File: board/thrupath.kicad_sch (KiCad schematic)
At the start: 114 parts, among them J6 BEL_FUSE_0826-1G1T-23-F, J7 BEL_FUSE_0826-1G1T-23-F, U4 XC7S15-1FTGB196C, U5 KSZ9031RN, U6 KSZ9031RN, U7 ECS-2016MVQ-250-CN-TR, U8 ECS-2016MVQ-250-CN-TR

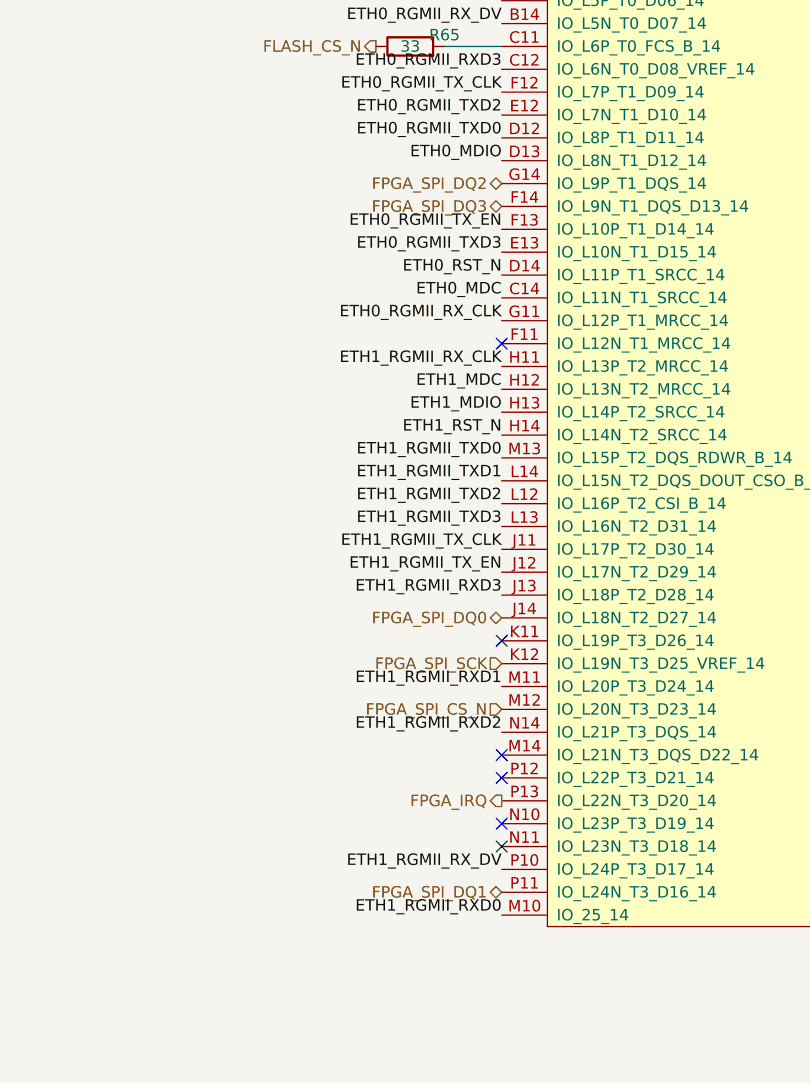
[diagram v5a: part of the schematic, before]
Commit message: Updating file: ethernet-tap.kicad_pcb with current fully routed design.
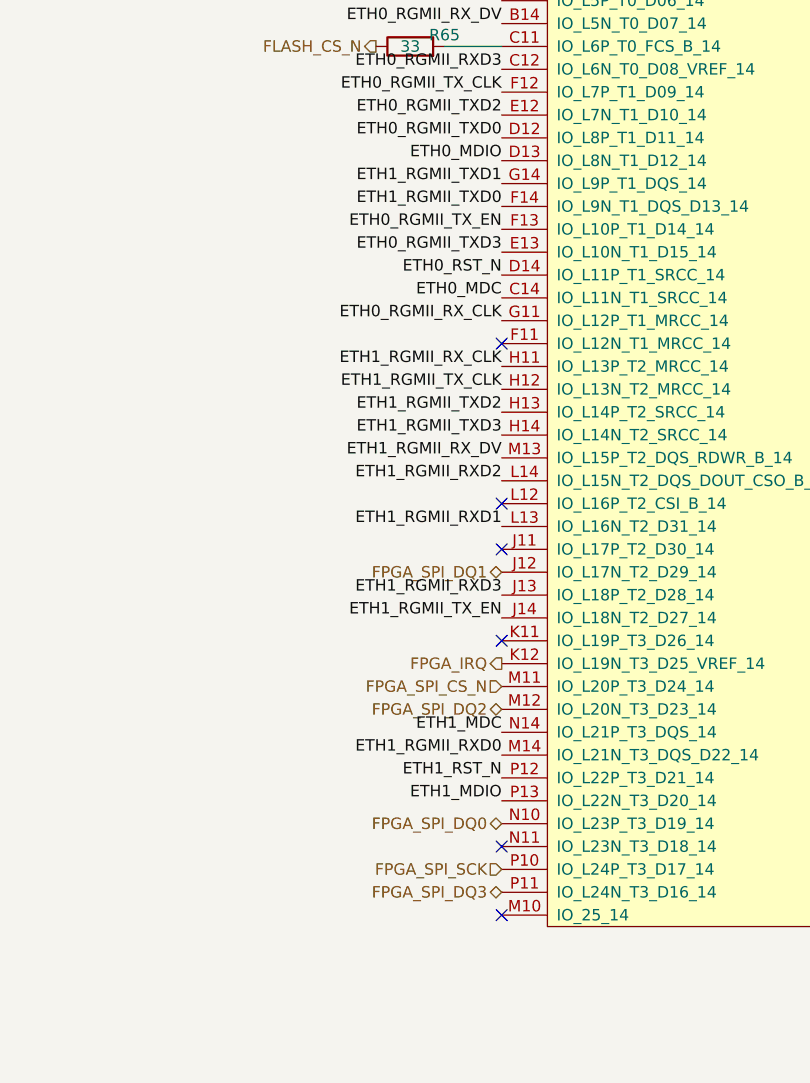
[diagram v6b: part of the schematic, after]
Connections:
- net ETH1_MDC: now also U4.N14 (IO_L21P_T3_DQS_14); no longer U4.H12 (IO_L13N_T2_MRCC_14)
- net ETH1_MDIO: now also U4.P13 (IO_L22N_T3_D20_14); no longer U4.H13 (IO_L14P_T2_SRCC_14)
- net ETH1_RGMII_RXD0: now also U4.M14 (IO_L21N_T3_DQS_D22_14); no longer U4.M10 (IO_25_14)
- net ETH1_RGMII_RXD1: now also U4.L13 (IO_L16N_T2_D31_14); no longer U4.M11 (IO_L20P_T3_D24_14)
- net ETH1_RGMII_RXD2: now also U4.L14 (IO_L15N_T2_DQS_DOUT_CSO_B_14); no longer U4.N14 (IO_L21P_T3_DQS_14)
- net ETH1_RGMII_RX_DV: now also U4.M13 (IO_L15P_T2_DQS_RDWR_B_14); no longer U4.P10 (IO_L24P_T3_D17_14)
- net ETH1_RGMII_TXD0: now also U4.F14 (IO_L9N_T1_DQS_D13_14); no longer U4.M13 (IO_L15P_T2_DQS_RDWR_B_14)
- net ETH1_RGMII_TXD1: now also U4.G14 (IO_L9P_T1_DQS_14); no longer U4.L14 (IO_L15N_T2_DQS_DOUT_CSO_B_14)
- net ETH1_RGMII_TXD2: now also U4.H13 (IO_L14P_T2_SRCC_14); no longer U4.L12 (IO_L16P_T2_CSI_B_14)
- net ETH1_RGMII_TXD3: now also U4.H14 (IO_L14N_T2_SRCC_14); no longer U4.L13 (IO_L16N_T2_D31_14)
- net ETH1_RGMII_TX_CLK: now also U4.H12 (IO_L13N_T2_MRCC_14); no longer U4.J11 (IO_L17P_T2_D30_14)
- net ETH1_RGMII_TX_EN: now also U4.J14 (IO_L18N_T2_D27_14); no longer U4.J12 (IO_L17N_T2_D29_14)
- net ETH1_RST_N: now also U4.P12 (IO_L22P_T3_D21_14); no longer U4.H14 (IO_L14N_T2_SRCC_14)
- net FPGA_IRQ: now also U4.K12 (IO_L19N_T3_D25_VREF_14); no longer U4.P13 (IO_L22N_T3_D20_14)
- net FPGA_SPI_CS_N: now also U4.M11 (IO_L20P_T3_D24_14); no longer U4.M12 (IO_L20N_T3_D23_14)
- net FPGA_SPI_DQ0: now also U4.N10 (IO_L23P_T3_D19_14); no longer U4.J14 (IO_L18N_T2_D27_14)
- net FPGA_SPI_DQ1: now also U4.J12 (IO_L17N_T2_D29_14); no longer U4.P11 (IO_L24N_T3_D16_14)
- net FPGA_SPI_DQ2: now also U4.M12 (IO_L20N_T3_D23_14); no longer U4.G14 (IO_L9P_T1_DQS_14)
- net FPGA_SPI_DQ3: now also U4.P11 (IO_L24N_T3_D16_14); no longer U4.F14 (IO_L9N_T1_DQS_D13_14)
- net FPGA_SPI_SCK: now also U4.P10 (IO_L24P_T3_D17_14); no longer U4.K12 (IO_L19N_T3_D25_VREF_14)
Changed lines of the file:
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@@
   (title_block
     (title "Active 10/100/1000baseT Tap")
-    (date "2022-12-24")
+    (date "2022-12-26")
     (rev "0.1")
     (company "Antikernel Labs")
@@
   )
   (no_connect (at 143.51 165.1))
+  (no_connect (at 364.49 99.06))
+  (no_connect (at 364.49 137.16))
   (no_connect (at 143.51 176.53))
-  (no_connect (at 364.49 134.62))
   (no_connect (at 143.51 87.63))
   (no_connect (at 364.49 35.56))
-  (no_connect (at 364.49 127))
-  (no_connect (at 364.49 129.54))
   (no_connect (at 364.49 114.3))
-  (no_connect (at 364.49 137.16))
+  (no_connect (at 364.49 104.14))
   (no_connect (at 364.49 81.28))
   (no_connect (at 86.36 157.48))
+  (no_connect (at 364.49 144.78))
   (no_connect (at 364.49 33.02))
   (no_connect (at 143.51 76.2))
@@
     (effects (font (size 1.27 1.27)) (justify left bottom))
   )
-  (label "ETH1_RGMII_TXD1" (at 364.49 96.52 180)
+  (label "ETH1_RGMII_TXD1" (at 364.49 63.5 180)
     (effects (font (size 1.27 1.27)) (justify right bottom))
   )
@@
     (effects (font (size 1.27 1.27)) (justify left bottom))
   )
-  (label "ETH1_RGMII_TX_CLK" (at 364.49 104.14 180)
+  (label "ETH1_RGMII_TX_CLK" (at 364.49 86.36 180)
     (effects (font (size 1.27 1.27)) (justify right bottom))
   )
@@
     (effects (font (size 1.27 1.27)) (justify right bottom))
   )
-  (label "ETH1_RST_N" (at 364.49 91.44 180)
+  (label "ETH1_RST_N" (at 364.49 129.54 180)
     (effects (font (size 1.27 1.27)) (justify right bottom))
   )
@@
     (effects (font (size 1.27 1.27)) (justify left bottom))
   )
-  (label "ETH1_RGMII_TXD0" (at 364.49 93.98 180)
+  (label "ETH1_RGMII_TXD0" (at 364.49 66.04 180)
     (effects (font (size 1.27 1.27)) (justify right bottom))
   )
@@
     (effects (font (size 1.27 1.27)) (justify right bottom))
   )
-  (label "ETH1_RGMII_RXD2" (at 364.49 124.46 180)
+  (label "ETH1_RGMII_RXD2" (at 364.49 96.52 180)
     (effects (font (size 1.27 1.27)) (justify right bottom))
   )
@@
     (effects (font (size 1.27 1.27)) (justify right bottom))
   )
-  (label "ETH1_MDC" (at 364.49 86.36 180)
+  (label "ETH1_MDC" (at 364.49 124.46 180)
     (effects (font (size 1.27 1.27)) (justify right bottom))
   )
@@
     (effects (font (size 1.27 1.27)) (justify right bottom))
   )
-  (label "ETH1_RGMII_RX_DV" (at 364.49 139.7 180)
+  (label "ETH1_RGMII_RX_DV" (at 364.49 93.98 180)
     (effects (font (size 1.27 1.27)) (justify right bottom))
   )
@@
     (effects (font (size 1.27 1.27)) (justify right bottom))
   )
-  (label "ETH1_RGMII_RXD1" (at 364.49 119.38 180)
+  (label "ETH1_RGMII_RXD1" (at 364.49 101.6 180)
     (effects (font (size 1.27 1.27)) (justify right bottom))
   )
@@
     (effects (font (size 1.27 1.27)) (justify left bottom))
   )
-  (label "ETH1_MDIO" (at 364.49 88.9 180)
+  (label "ETH1_MDIO" (at 364.49 132.08 180)
     (effects (font (size 1.27 1.27)) (justify right bottom))
   )
@@
     (effects (font (size 1.27 1.27)) (justify left bottom))
   )
-  (label "ETH1_RGMII_TX_EN" (at 364.49 106.68 180)
-    (effects (font (size 1.27 1.27)) (justify right bottom))
-  )
-  (label "ETH1_RGMII_TXD3" (at 364.49 101.6 180)
+  (label "ETH1_RGMII_TX_EN" (at 364.49 111.76 180)
+    (effects (font (size 1.27 1.27)) (justify right bottom))
+  )
+  (label "ETH1_RGMII_TXD3" (at 364.49 91.44 180)
     (effects (font (size 1.27 1.27)) (justify right bottom))
   )
@@
     (effects (font (size 1.27 1.27)) (justify right bottom))
   )
-  (label "ETH1_RGMII_TXD2" (at 364.49 99.06 180)
+  (label "ETH1_RGMII_TXD2" (at 364.49 88.9 180)
     (effects (font (size 1.27 1.27)) (justify right bottom))
   )
@@
     (effects (font (size 1.27 1.27)) (justify right bottom))
   )
-  (label "ETH1_RGMII_RXD0" (at 364.49 144.78 180)
+  (label "ETH1_RGMII_RXD0" (at 364.49 127 180)
     (effects (font (size 1.27 1.27)) (justify right bottom))
   )
@@
     (effects (font (size 1.27 1.27)) (justify right))
   )
-  (hierarchical_label "FPGA_SPI_CS_N" (shape input) (at 364.49 121.92 180)
+  (hierarchical_label "FPGA_SPI_CS_N" (shape input) (at 364.49 119.38 180)
     (effects (font (size 1.27 1.27)) (justify right))
   )
@@
     (effects (font (size 1.27 1.27)) (justify right))
   )
-  (hierarchical_label "FPGA_SPI_DQ2" (shape bidirectional) (at 364.49 63.5 180)
+  (hierarchical_label "FPGA_SPI_DQ2" (shape bidirectional) (at 364.49 121.92 180)
     (effects (font (size 1.27 1.27)) (justify right))
   )
-  (hierarchical_label "FPGA_SPI_DQ3" (shape bidirectional) (at 364.49 66.04 180)
+  (hierarchical_label "FPGA_SPI_DQ3" (shape bidirectional) (at 364.49 142.24 180)
     (effects (font (size 1.27 1.27)) (justify right))
   )
-  (hierarchical_label "FPGA_SPI_SCK" (shape input) (at 364.49 116.84 180)
+  (hierarchical_label "FPGA_SPI_SCK" (shape input) (at 364.49 139.7 180)
     (effects (font (size 1.27 1.27)) (justify right))
   )
-  (hierarchical_label "FPGA_IRQ" (shape output) (at 364.49 132.08 180)
+  (hierarchical_label "FPGA_IRQ" (shape output) (at 364.49 116.84 180)
     (effects (font (size 1.27 1.27)) (justify right))
   )
@@
     (effects (font (size 1.27 1.27)) (justify right))
   )
-  (hierarchical_label "FPGA_SPI_DQ1" (shape bidirectional) (at 364.49 142.24 180)
+  (hierarchical_label "FPGA_SPI_DQ1" (shape bidirectional) (at 364.49 106.68 180)
     (effects (font (size 1.27 1.27)) (justify right))
   )
-  (hierarchical_label "FPGA_SPI_DQ0" (shape bidirectional) (at 364.49 111.76 180)
+  (hierarchical_label "FPGA_SPI_DQ0" (shape bidirectional) (at 364.49 134.62 180)
     (effects (font (size 1.27 1.27)) (justify right))
   )

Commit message: Final v0.1 layout after design review
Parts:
- added C187: 0.47 uF, azonenberg_pcb:EIA_0402_CAP_NOSILK, symbol device:C
- added J12: SMA, azonenberg_pcb:CONN_SMA_EDGE_SAMTEC_SMA_J_P_H_ST_EM1, symbol conn:CONN_COAXIAL
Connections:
- net 3V3: now also C187.1
- net GND: now also C187.2, J12.2 (Ext)
- net TRIG_OUT: now reaches U4.L12 (IO_L16P_T2_CSI_B_14)
- net TRIG_OUT: now also J12.1 (In)
- no-connect marks 14 -> 13
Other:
- note added: "Stitching caps for layer changes"
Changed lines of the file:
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@@
   (title_block
     (title "Active 10/100/1000baseT Tap")
-    (date "2022-12-26")
+    (date "2022-12-27")
     (rev "0.1")
     (company "Antikernel Labs")
@@
   )
   (no_connect (at 143.51 165.1))
-  (no_connect (at 364.49 99.06))
   (no_connect (at 364.49 137.16))
   (no_connect (at 143.51 176.53))
@@
     (stroke (width 0) (type default) (color 0 0 0 0))
   )
+  (wire (pts (xy 280.67 97.79) (xy 284.48 97.79))
+    (stroke (width 0) (type default) (color 0 0 0 0))
+  )
   (wire (pts (xy 143.51 118.11) (xy 148.59 118.11))
     (stroke (width 0) (type default) (color 0 0 0 0))
@@
     (effects (font (size 1.27 1.27)) (justify left bottom))
   )
+  (text "Stitching caps for layer changes" (at 20.32 266.7 0)
+    (effects (font (size 1.27 1.27)) (justify left bottom))
+  )
   (text "Strap: PHYADDR[2] = 0" (at 204.47 72.39 0)
     (effects (font (size 1.27 1.27)) (justify left bottom))
@@
     (effects (font (size 1.27 1.27)) (justify right bottom))
   )
+  (label "3V3" (at 21.59 256.54 180)
+    (effects (font (size 1.27 1.27)) (justify right bottom))
+  )
   (label "ETH0_MDC" (at 143.51 71.12 0)
     (effects (font (size 1.27 1.27)) (justify left bottom))
@@
     (effects (font (size 1.27 1.27)) (justify left bottom))
   )
+  (label "GND" (at 280.67 97.79 180)
+    (effects (font (size 1.27 1.27)) (justify right bottom))
+  )
   (label "ETH0_D_N" (at 39.37 76.2 0)
     (effects (font (size 1.27 1.27)) (justify left bottom))
@@
     (effects (font (size 1.27 1.27)) (justify right bottom))
   )
+  (label "TRIG_OUT" (at 280.67 92.71 180)
+    (effects (font (size 1.27 1.27)) (justify right bottom))
+  )
+  (label "GND" (at 21.59 264.16 180)
+    (effects (font (size 1.27 1.27)) (justify right bottom))
+  )
   (label "GND" (at 21.59 243.84 180)
     (effects (font (size 1.27 1.27)) (justify right bottom))
@@
   )
   (label "1V2" (at 279.4 207.01 180)
+    (effects (font (size 1.27 1.27)) (justify right bottom))
+  )
+  (label "TRIG_OUT" (at 364.49 99.06 180)
     (effects (font (size 1.27 1.27)) (justify right bottom))
   )
@@
     (pin "2")
   )
+  (symbol (lib_id "device:C") (at 21.59 260.35 0) (unit 1)
+    (in_bom yes) (on_board yes)
+    (property "Reference" "C187" (id 0) (at 24.511 259.1816 0)
+      (effects (font (size 1.27 1.27)) (justify left))
+    )
+    (property "Value" "0.47 uF" (id 1) (at 24.511 261.493 0)
+      (effects (font (size 1.27 1.27)) (justify left))
+    )
+    (property "Footprint" "azonenberg_pcb:EIA_0402_CAP_NOSILK" (id 2) (at 22.5552 264.16 0)
+      (effects (font (size 1.27 1.27)) hide)
+    )
+    (property "Datasheet" "" (id 3) (at 21.59 260.35 0)
+      (effects (font (size 1.27 1.27)) hide)
+    )
+    (pin "1")
+    (pin "2")
+  )
   (symbol (lib_id "device:R") (at 354.33 30.48 90) (unit 1)
     (in_bom yes) (on_board yes)
@@
       (effects (font (size 1.27 1.27)) hide)
     )
+    (pin "1")
+    (pin "2")
+  )
+  (symbol (lib_id "conn:CONN_COAXIAL") (at 284.48 92.71 0) (unit 1)
+    (in_bom yes) (on_board yes) (fields_autoplaced)
+    (property "Reference" "J12" (id 0) (at 287.0201 92.0947 0)
+      (effects (font (size 1.27 1.27)) (justify left))
+    )
+    (property "Value" "SMA" (id 1) (at 287.0201 94.8698 0)
+      (effects (font (size 1.27 1.27)) (justify left))
+    )
+    (property "Footprint" "azonenberg_pcb:CONN_SMA_EDGE_SAMTEC_SMA_J_P_H_ST_EM1" (id 2) (at 284.48 92.71 0)
+      (effects (font (size 1.27 1.27)) hide)
+    )
+    (property "Datasheet" "" (id 3) (at 284.48 92.71 0)
+      (effects (font (size 1.27 1.27)) hide)
+    )
